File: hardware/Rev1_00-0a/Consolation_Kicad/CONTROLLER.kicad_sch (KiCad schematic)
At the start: 73 parts, among them J11 5051102291, J13 5051102291, J14 61300311121, J15 61300311121, Q18 SSM3K56FS,LF, U2 RP2350A, U8 GD25Q32CWIGR, Y1 12MHz 10pF

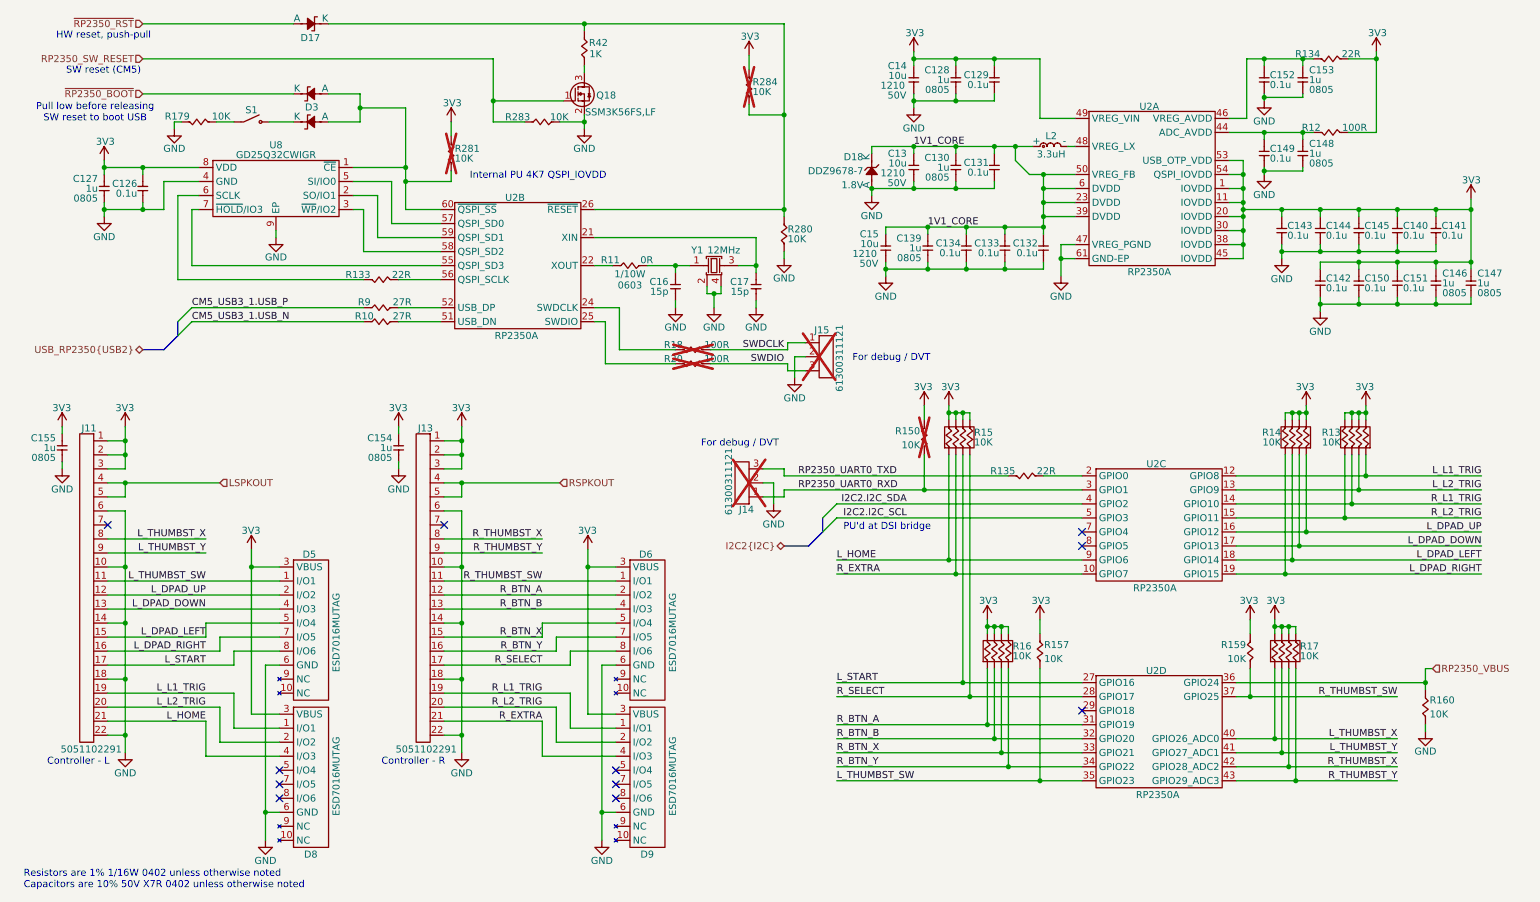
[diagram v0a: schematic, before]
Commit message: Preliminary placement of Consolation continues
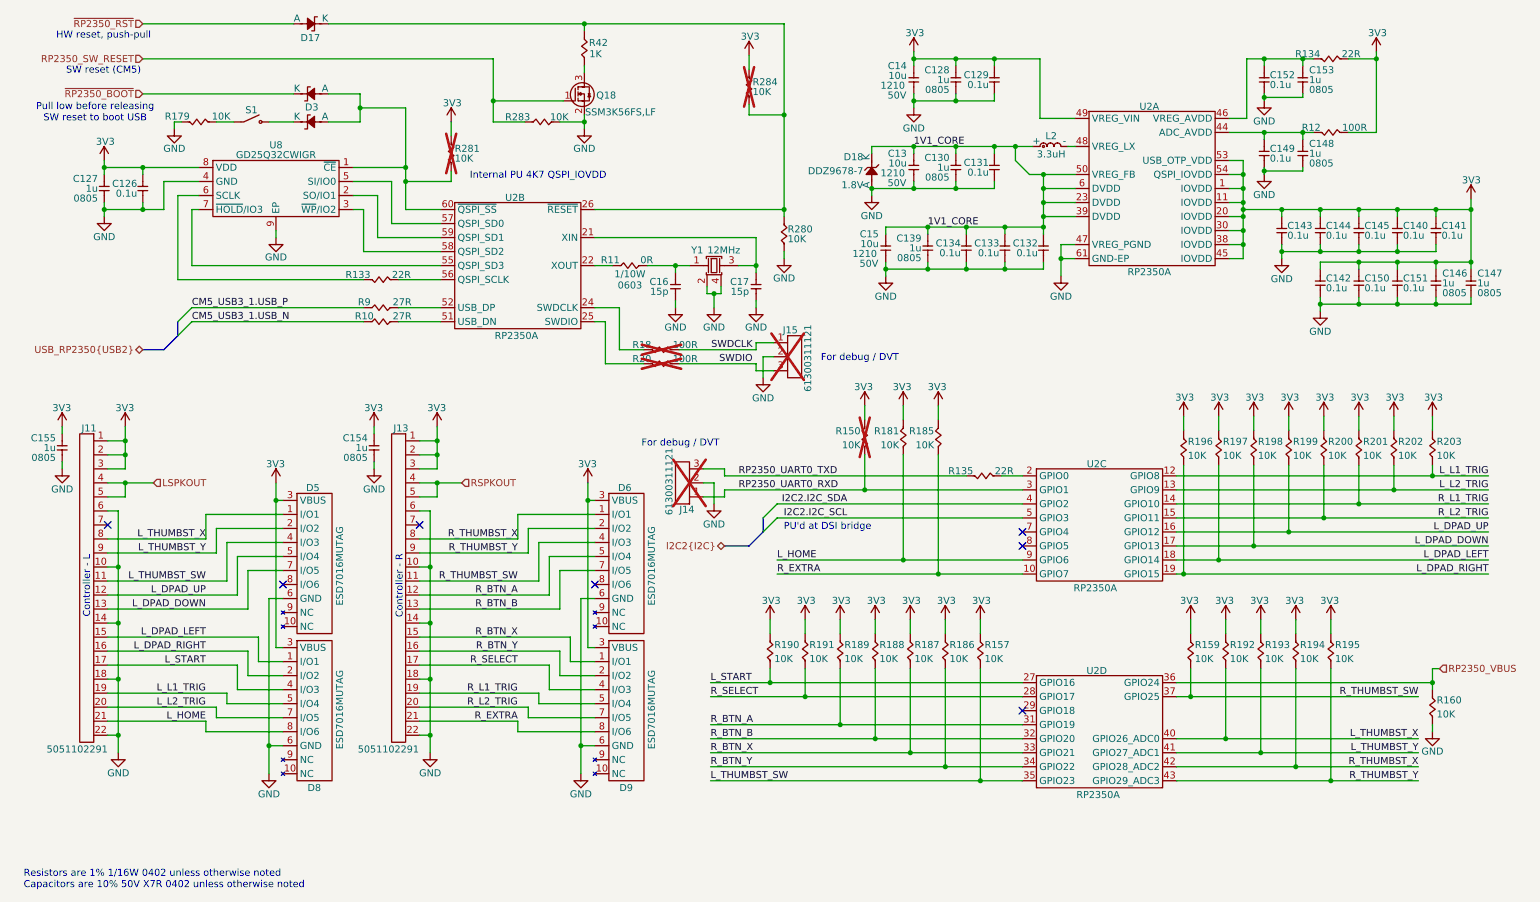
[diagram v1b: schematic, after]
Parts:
- removed R13, R14, R15, R16, R17: 10K, footprint:RES_ARRAY_4_1206, symbol KicadCompDb:Resistors/RES_SMT_00037
- added R181, R185, R186, R187, R188, R189, R190, R191, R192, R193, R194, R195, R196, R197, R198, R199, R200, R201, R202, R203: 10K, footprint:RES_0402, symbol KicadCompDb:Resistors/RES_SMT_00013
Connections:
- net 3V3: now also R181.2, R185.2, R186.2, R187.2, R188.2, R189.2, R190.2, R191.2, R192.2, R193.2, R194.2, R195.2, R196.2, R197.2, R198.2, R199.2, R200.2, R201.2, R202.2, R203.2
- net L_DPAD_DOWN: now also D5.7 (I/O5), R198.1; no longer D5.4 (I/O3)
- net L_DPAD_LEFT: now also D8.1 (I/O1), R197.1; no longer D5.5 (I/O4)
- net L_DPAD_RIGHT: now also D8.2 (I/O2), R196.1; no longer D5.7 (I/O5)
- net L_DPAD_UP: now also D5.5 (I/O4), R199.1; no longer D5.2 (I/O2)
- net L_HOME: now also D8.8 (I/O6), R181.1; no longer D8.4 (I/O3)
- net L_L1_TRIG: now also D8.5 (I/O4), R203.1; no longer D8.1 (I/O1)
- net L_L2_TRIG: now also D8.7 (I/O5), R202.1; no longer D8.2 (I/O2)
- net L_START: now also D8.4 (I/O3), R190.1; no longer D5.8 (I/O6)
- net L_THUMBST_SW: now also D5.4 (I/O3); no longer D5.1 (I/O1)
- net L_THUMBST_X: now also D5.1 (I/O1), R192.1
- net L_THUMBST_Y: now also D5.2 (I/O2), R193.1
- net R_BTN_A: now also D6.5 (I/O4), R189.1; no longer D6.2 (I/O2)
- net R_BTN_B: now also D6.7 (I/O5), R188.1; no longer D6.4 (I/O3)
- net R_BTN_X: now also D9.1 (I/O1), R187.1; no longer D6.5 (I/O4)
- net R_BTN_Y: now also D9.2 (I/O2), R186.1; no longer D6.7 (I/O5)
- net R_EXTRA: now also D9.8 (I/O6), R185.1; no longer D9.4 (I/O3)
- net R_L1_TRIG: now also D9.5 (I/O4), R201.1; no longer D9.1 (I/O1)
- net R_L2_TRIG: now also D9.7 (I/O5), R200.1; no longer D9.2 (I/O2)
- net R_SELECT: now also D9.4 (I/O3), R191.1; no longer D6.8 (I/O6)
- net R_THUMBST_SW: now also D6.4 (I/O3); no longer D6.1 (I/O1)
- net R_THUMBST_X: now also D6.1 (I/O1), R194.1
- net R_THUMBST_Y: now also D6.2 (I/O2), R195.1
- no-connect marks 11 -> 7
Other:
- moved on the sheet: C154, D5, D6, D8, D9, J13, J14, J15, R135, R150, R157, R159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

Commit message: Work on preliminary placement + RP2350A fanout
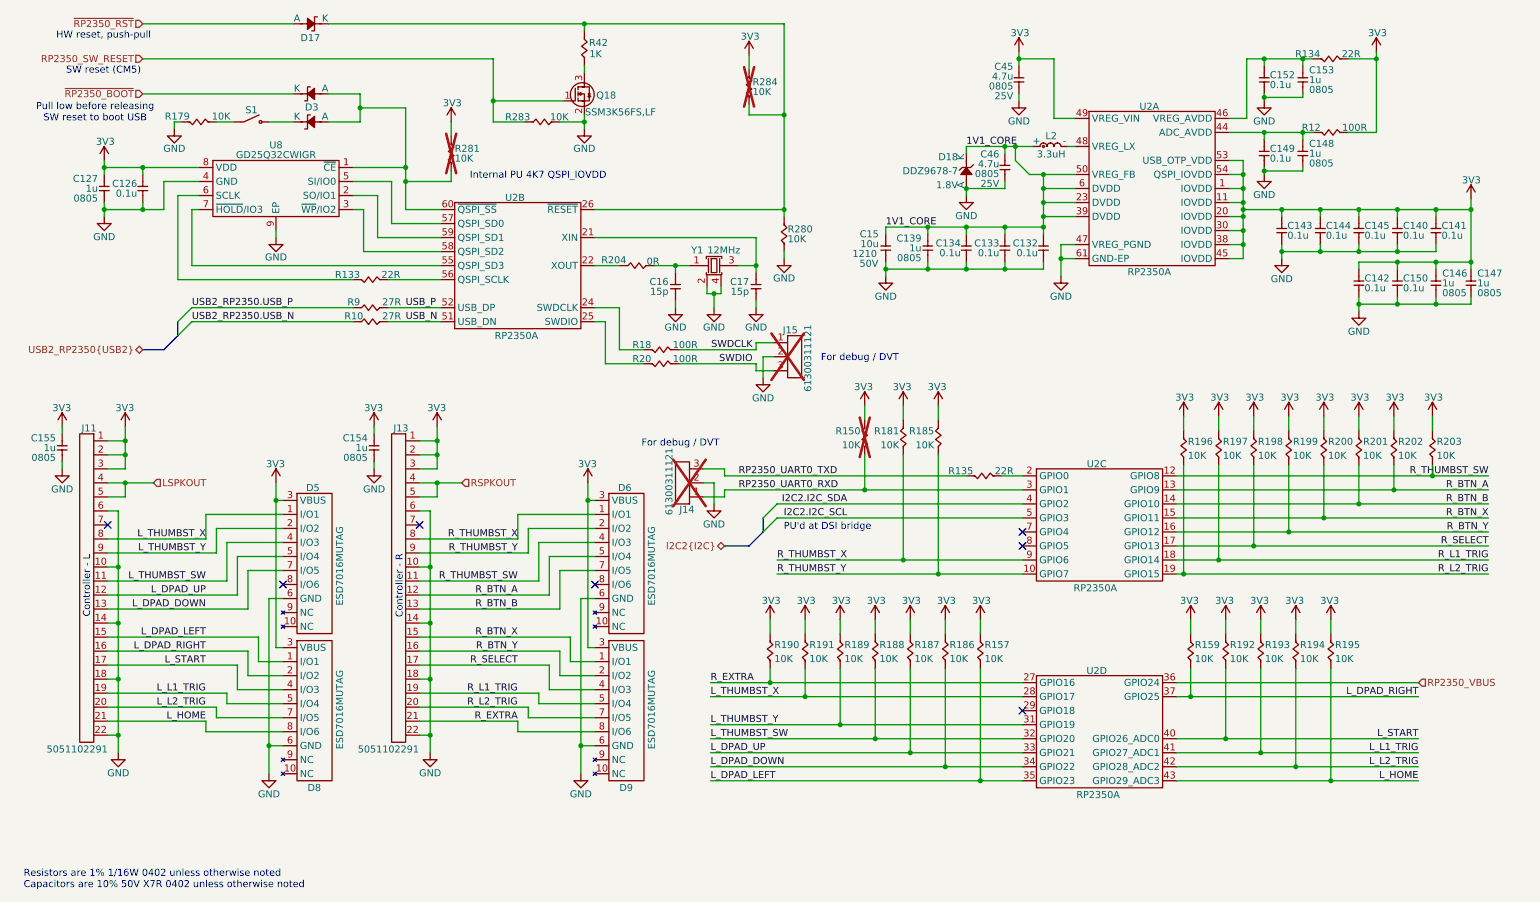
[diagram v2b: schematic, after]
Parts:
- removed C128, C130: 1u, footprint:CAP_NONPOL_0805, symbol KicadCompDb:Capacitors/CAP_CER_SMT_00002
- removed C129, C131, C151: 0.1u, footprint:CAP_NONPOL_0402, symbol KicadCompDb:Capacitors/CAP_CER_SMT_00001
- removed C13, C14: 10u, footprint:CAP_NONPOL_1210, symbol KicadCompDb:Capacitors/CAP_CER_SMT_00014
- removed R11: 0R, footprint:RES_0603, symbol KicadCompDb:Resistors/RES_SMT_00021
- removed R160: 10K, footprint:RES_0402, symbol KicadCompDb:Resistors/RES_SMT_00013
- added C45, C46: 4.7u, footprint:CAP_NONPOL_0805, symbol KicadCompDb:Capacitors/CAP_CER_SMT_00017
- added R204: 0R, footprint:RES_0402, symbol KicadCompDb:Resistors/RES_SMT_00001
- R18, R20: now fitted
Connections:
- net 1V1_CORE: now also C46.1
- net 3V3: now also C45.1
- net GND: now also C45.2, C46.2
- net L_DPAD_DOWN: now also R186.1, U2.34 (GPIO22); no longer R198.1, U2.17 (GPIO13)
- net L_DPAD_LEFT: now also R157.1, U2.35 (GPIO23); no longer R197.1, U2.18 (GPIO14)
- net L_DPAD_RIGHT: now also R159.1, U2.37 (GPIO25); no longer R196.1, U2.19 (GPIO15)
- net L_DPAD_UP: now also R187.1, U2.33 (GPIO21); no longer R199.1, U2.16 (GPIO12)
- net L_HOME: now also R195.1, U2.43 (GPIO29_ADC3); no longer R181.1, U2.9 (GPIO6)
- net L_L1_TRIG: now also R193.1, U2.41 (GPIO27_ADC1); no longer R203.1, U2.12 (GPIO8)
- net L_L2_TRIG: now also R194.1, U2.42 (GPIO28_ADC2); no longer R202.1, U2.13 (GPIO9)
- net L_START: now also R192.1, U2.40 (GPIO26_ADC0); no longer R190.1, U2.27 (GPIO16)
- net L_THUMBST_SW: now also R188.1, U2.32 (GPIO20); no longer R157.1, U2.35 (GPIO23)
- net L_THUMBST_X: now also R191.1, U2.28 (GPIO17); no longer R192.1, U2.40 (GPIO26_ADC0)
- net L_THUMBST_Y: now also R189.1, U2.31 (GPIO19); no longer R193.1, U2.41 (GPIO27_ADC1)
- net R_BTN_A: now also R202.1, U2.13 (GPIO9); no longer R189.1, U2.31 (GPIO19)
- net R_BTN_B: now also R201.1, U2.14 (GPIO10); no longer R188.1, U2.32 (GPIO20)
- net R_BTN_X: now also R200.1, U2.15 (GPIO11); no longer R187.1, U2.33 (GPIO21)
- net R_BTN_Y: now also R199.1, U2.16 (GPIO12); no longer R186.1, U2.34 (GPIO22)
- net R_EXTRA: now also R190.1, U2.27 (GPIO16); no longer R185.1, U2.10 (GPIO7)
- net R_L1_TRIG: now also R197.1, U2.18 (GPIO14); no longer R201.1, U2.14 (GPIO10)
- net R_L2_TRIG: now also R196.1, U2.19 (GPIO15); no longer R200.1, U2.15 (GPIO11)
- net R_SELECT: now also R198.1, U2.17 (GPIO13); no longer R191.1, U2.28 (GPIO17)
- net R_THUMBST_SW: now also R203.1, U2.12 (GPIO8); no longer R159.1, U2.37 (GPIO25)
- net R_THUMBST_X: now also R181.1, U2.9 (GPIO6); no longer R194.1, U2.42 (GPIO28_ADC2)
- net R_THUMBST_Y: now also R185.1, U2.10 (GPIO7); no longer R195.1, U2.43 (GPIO29_ADC3)
- net USB_N: now reaches R10.2, U2.51 (USB_DN)
- net at U2.22 (XOUT): now also R204.1
- net USB_P: now reaches R9.2, U2.52 (USB_DP)
- net at C16.2, Y1.1 (XI): now also R204.2
- net CM5_USB3_1.USB_N renamed USB2_RP2350.USB_N
- net CM5_USB3_1.USB_P renamed USB2_RP2350.USB_P
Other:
- moved on the sheet: C142, C150, D18, R10, R133, R9

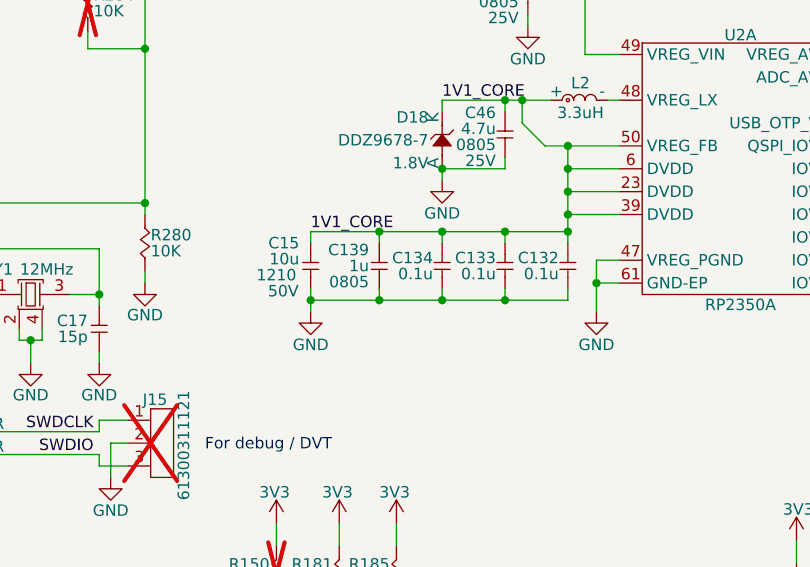
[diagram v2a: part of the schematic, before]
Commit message: Update ConJoy L2 trigger (2-level trigger instead) Update ConJoy all output files accordingly
Work on Consolation preliminary placement
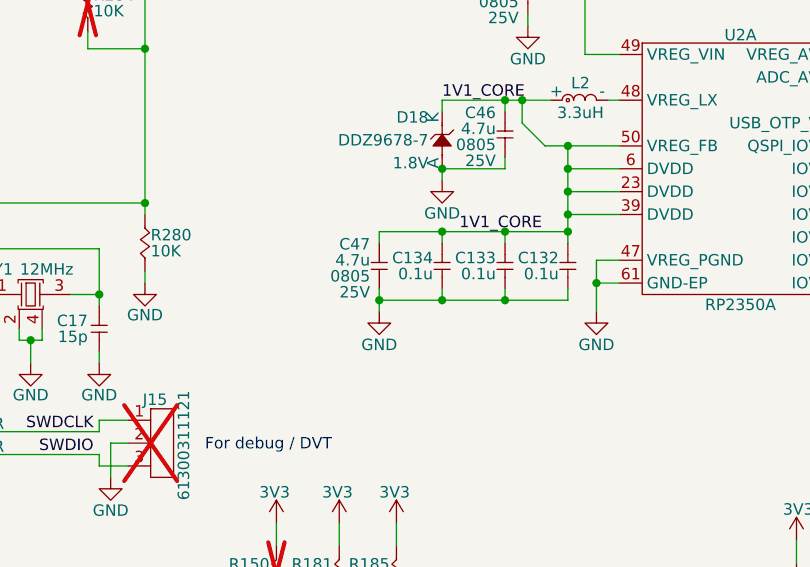
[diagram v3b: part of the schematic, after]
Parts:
- removed C139: 1u, footprint:CAP_NONPOL_0805, symbol KicadCompDb:Capacitors/CAP_CER_SMT_00002
- removed C15: 10u, footprint:CAP_NONPOL_1210, symbol KicadCompDb:Capacitors/CAP_CER_SMT_00014
- added C47: 4.7u, footprint:CAP_NONPOL_0805, symbol KicadCompDb:Capacitors/CAP_CER_SMT_00017
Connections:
- net 1V1_CORE: now also C47.1
- net GND: now also C47.2

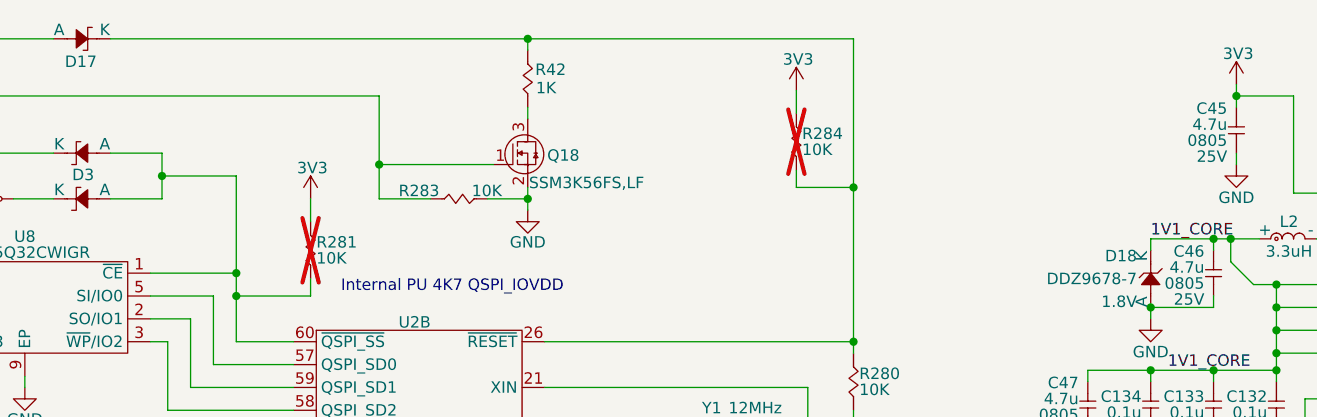
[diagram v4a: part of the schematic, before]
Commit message: Preliminary placement done Add test points to PCB
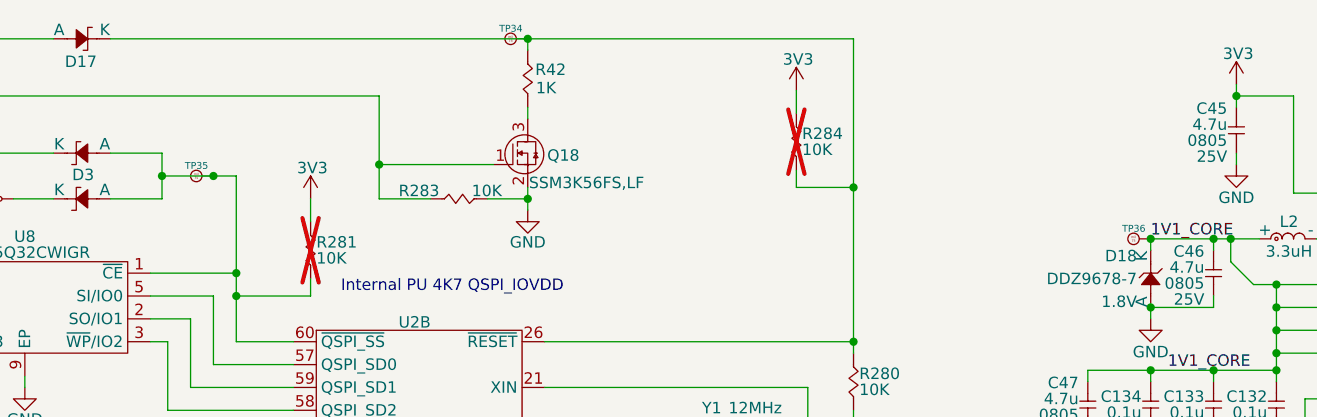
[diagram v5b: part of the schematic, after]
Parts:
- added TP34, TP35, TP36: 75 mils, footprint:SMT_TP_75_MILS, symbol KicadCompDb:Test Point/TP_00004
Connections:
- net 1V1_CORE: now also TP36.1
- net at D17.1 (K), R280.2, R284.1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: now also TP34.1
- net at D2.2 (A), D3.2 (A), R281.1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: now also TP35.1

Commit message: Preliminary routing
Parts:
- removed C45: 4.7u, footprint:CAP_NONPOL_0805, symbol KicadCompDb:Capacitors/CAP_CER_SMT_00017
- removed D18: DDZ9678-7, footprint:SOD-123, symbol KicadCompDb:Diodes/DIODE_00002
- added C32: 22u, footprint:CAP_NONPOL_0805, symbol KicadCompDb:Capacitors/CAP_CER_SMT_00011
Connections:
- net 3V3: now also C32.2
- net GND: now also C32.1
